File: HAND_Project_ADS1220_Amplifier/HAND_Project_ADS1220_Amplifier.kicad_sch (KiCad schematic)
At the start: 0 parts

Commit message: KiCad
need to assign footprints
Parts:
- added D1, D4: LED, LED_THT:LED_D3.0mm, symbol Device:LED
- added D2, D3: 1N5817, Diode_THT:D_DO-41_SOD81_P10.16mm_Horizontal, symbol Diode:1N5817
- added J1: Screw_Terminal_01x04, symbol Connector:Screw_Terminal_01x04
- added J2, J3: Conn_01x03_Pin, symbol Connector:Conn_01x03_Pin
- added R1, R2: 330, symbol Device:R
- added U1: ADS1220IPWR, ADS1220IPWR:SOP65P640X120-16N, symbol ADS1220IPWR:ADS1220IPWR
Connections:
- new net: D2.1 (K), R1.1, U1.13 (DVDD)
- new net: D1.2 (A), R1.2
- new net: D3.1 (K), R2.1, U1.12 (AVDD)
- new net: J2.1 (Pin_1), U1.1 (SCLK)
- new net: J2.2 (Pin_2), U1.2 (~{CS})
- new net: J2.3 (Pin_3), U1.3 (CLK)
- new net: D4.2 (A), R2.2
- new net: J1.1 (Pin_1), U1.10 (AIN1)
- new net: J1.2 (Pin_2), U1.11 (AIN0/REFP1)
- new net: J3.3 (Pin_3), U1.14 (~{DRDY})
- new net: J3.1 (Pin_1), U1.15 (DOUT/~{DRDY})
- new net: J3.2 (Pin_2), U1.16 (DIN)
- new net 3.3V: D2.2 (A)
- new net 5V: D3.2 (A), J1.4 (Pin_4)
- new net GND: D1.1 (K), D4.1 (K), J1.3 (Pin_3), U1.4 (DGND), U1.5 (AVSS)
- no-connect marks 0 -> 2
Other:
- note added: "4.096MHz PWM 50% Duty Cycle"
- note added: "Pin Connector for Strain Gauge"

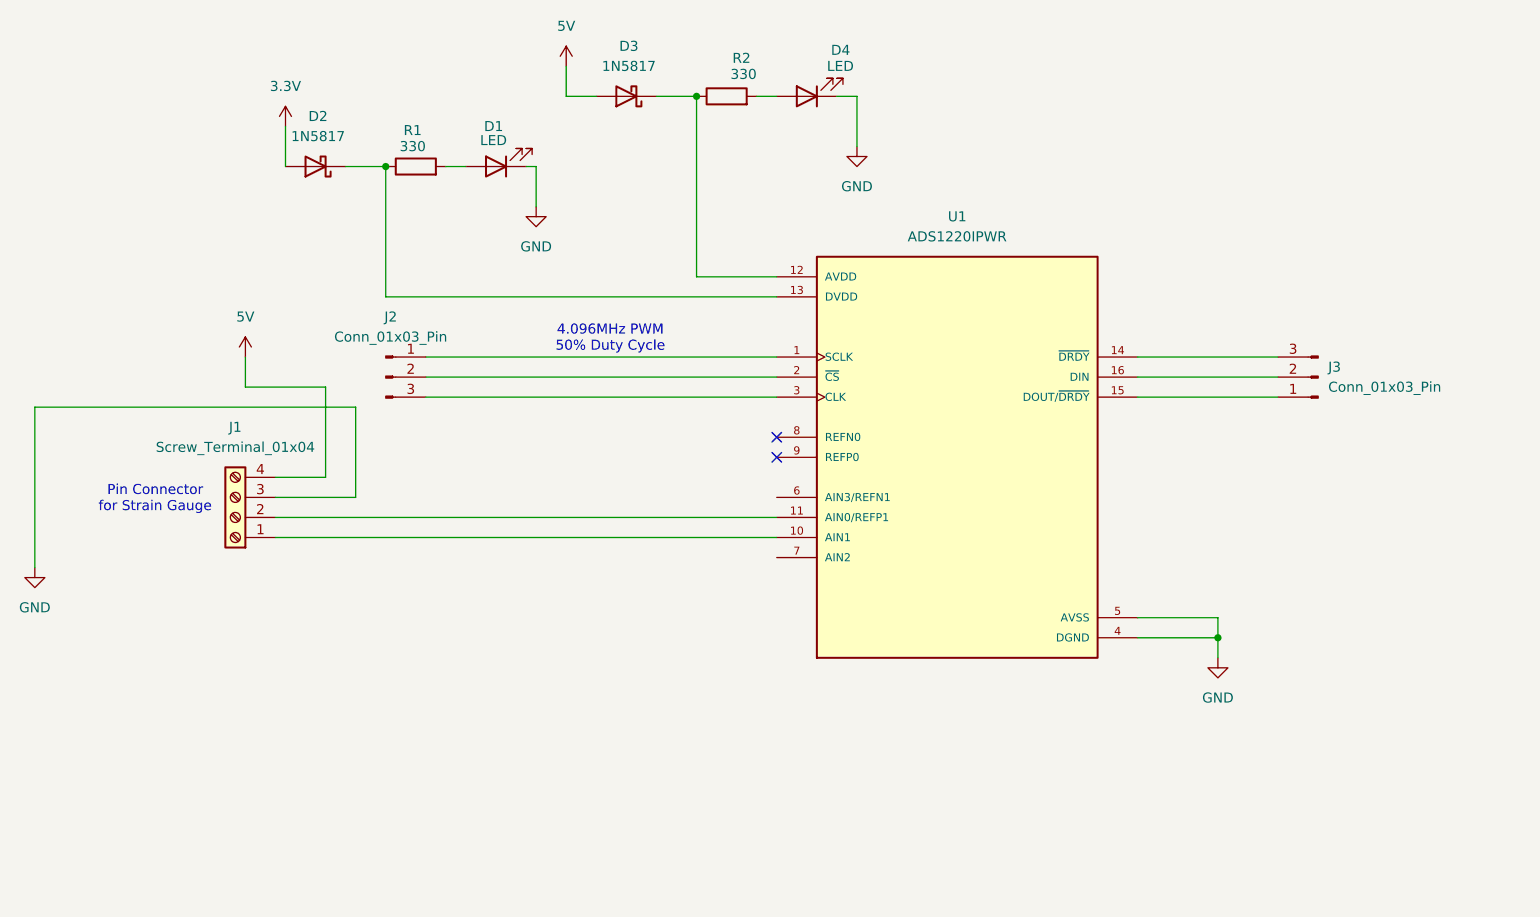
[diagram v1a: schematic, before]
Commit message: Finished schematics + footprints
Need to work on actual PCB design
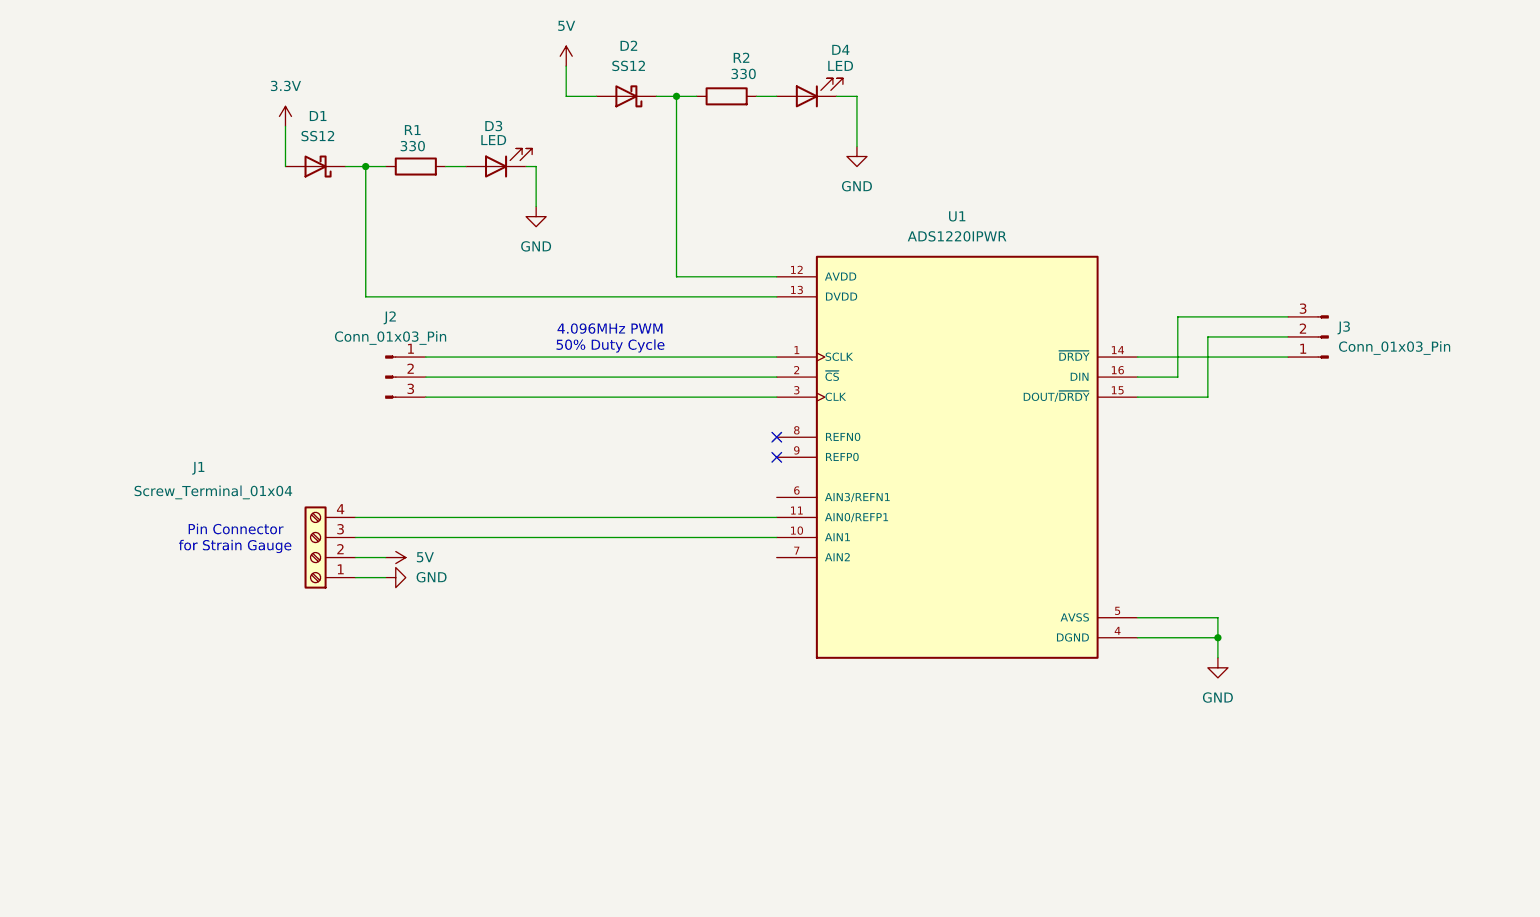
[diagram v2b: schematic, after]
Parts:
- removed D2, D3: 1N5817, Diode_THT:D_DO-41_SOD81_P10.16mm_Horizontal, symbol Diode:1N5817
- added D1, D2: SS12, Diode_SMD:D_SMA, symbol Diode:SS12
- D3: renamed from D1; footprint LED_THT:LED_D3.0mm -> LED_SMD:LED_0603_1608Metric_Pad1.05x0.95mm_HandSolder
- D4: footprint LED_THT:LED_D3.0mm -> LED_SMD:LED_0603_1608Metric_Pad1.05x0.95mm_HandSolder
- J1: footprint (none) -> TerminalBlock_Phoenix:TerminalBlock_Phoenix_MKDS-1,5-4_1x04_P5.00mm_Horizontal
- J2, J3: footprint (none) -> Connector_PinHeader_2.54mm:PinHeader_1x03_P2.54mm_Vertical
- R1, R2: footprint (none) -> Resistor_SMD:R_0603_1608Metric_Pad0.98x0.95mm_HandSolder
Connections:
- net 3.3V: now also D1.2 (A)
- net 5V: now also J1.2 (Pin_2), D2.2 (A); no longer J1.4 (Pin_4)
- net GND: now also J1.1 (Pin_1); no longer J1.3 (Pin_3)
- net at R1.1, U1.13 (DVDD): now also D1.1 (K)
- net at R2.1, U1.12 (AVDD): now also D2.1 (K)
- net at U1.10 (AIN1): now also J1.3 (Pin_3); no longer J1.1 (Pin_1)
- net at U1.11 (AIN0/REFP1): now also J1.4 (Pin_4); no longer J1.2 (Pin_2)
- net at U1.14 (~{DRDY}): now also J3.1 (Pin_1); no longer J3.3 (Pin_3)
- net at U1.15 (DOUT/~{DRDY}): now also J3.2 (Pin_2); no longer J3.1 (Pin_1)
- net at U1.16 (DIN): now also J3.3 (Pin_3); no longer J3.2 (Pin_2)
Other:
- moved on the sheet: J1, J3

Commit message: pin? idk
stuff
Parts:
- J2, J3: footprint Connector_PinHeader_2.54mm:PinHeader_1x03_P2.54mm_Vertical -> Connector_PinSocket_1.00mm:PinSocket_1x03_P1.00mm_Vertical
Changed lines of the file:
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@@
 			)
 		)
-		(property "Footprint" "Connector_PinHeader_2.54mm:PinHeader_1x03_P2.54mm_Vertical"
+		(property "Footprint" "Connector_PinSocket_1.00mm:PinSocket_1x03_P1.00mm_Vertical"
 			(at 76.2 78.74 0)
 			(effects
@@
 			)
 		)
-		(property "Footprint" "Connector_PinHeader_2.54mm:PinHeader_1x03_P2.54mm_Vertical"
+		(property "Footprint" "Connector_PinSocket_1.00mm:PinSocket_1x03_P1.00mm_Vertical"
 			(at 195.58 73.66 0)
 			(effects

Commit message: 4 PM meeting
stuff
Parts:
- added J4: Conn_01x03_Pin, Connector:FanPinHeader_1x03_P2.54mm_Vertical, symbol Connector:Conn_01x03_Pin
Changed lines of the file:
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@@
+	)
+	(symbol
+		(lib_id "Connector:Conn_01x03_Pin")
+		(at 210.82 92.71 0)
+		(unit 1)
+		(exclude_from_sim no)
+		(in_bom yes)
+		(on_board yes)
+		(dnp no)
+		(fields_autoplaced yes)
+		(property "Reference" "J4"
+			(at 211.455 85.09 0)
+			(effects
+				(font
+					(size 1.27 1.27)
+				)
+			)
+		)
+		(property "Value" "Conn_01x03_Pin"
+			(at 211.455 87.63 0)
+			(effects
+				(font
+					(size 1.27 1.27)
+				)
+			)
+		)
+		(property "Footprint" "Connector:FanPinHeader_1x03_P2.54mm_Vertical"
+			(at 210.82 92.71 0)
+			(effects
+				(font
+					(size 1.27 1.27)
+				)
+				(hide yes)
+			)
+		)
+		(property "Datasheet" "~"
+			(at 210.82 92.71 0)
+			(effects
+				(font
+					(size 1.27 1.27)
+				)
+				(hide yes)
+			)
+		)
+		(property "Description" "Generic connector, single row, 01x03, script generated"
+			(at 210.82 92.71 0)
+			(effects
+				(font
+					(size 1.27 1.27)
+				)
+				(hide yes)
+			)
+		)
+		(pin "3"
+		)
+		(pin "1"
+		)
+		(pin "2"
+		)
+		(instances
+			(project ""
+				(path "/f939b9ff-c66a-4ae1-bae0-ab02f1d8a589"
+					(reference "J4")
+					(unit 1)
+				)
+			)
+		)
 	)
 	(symbol

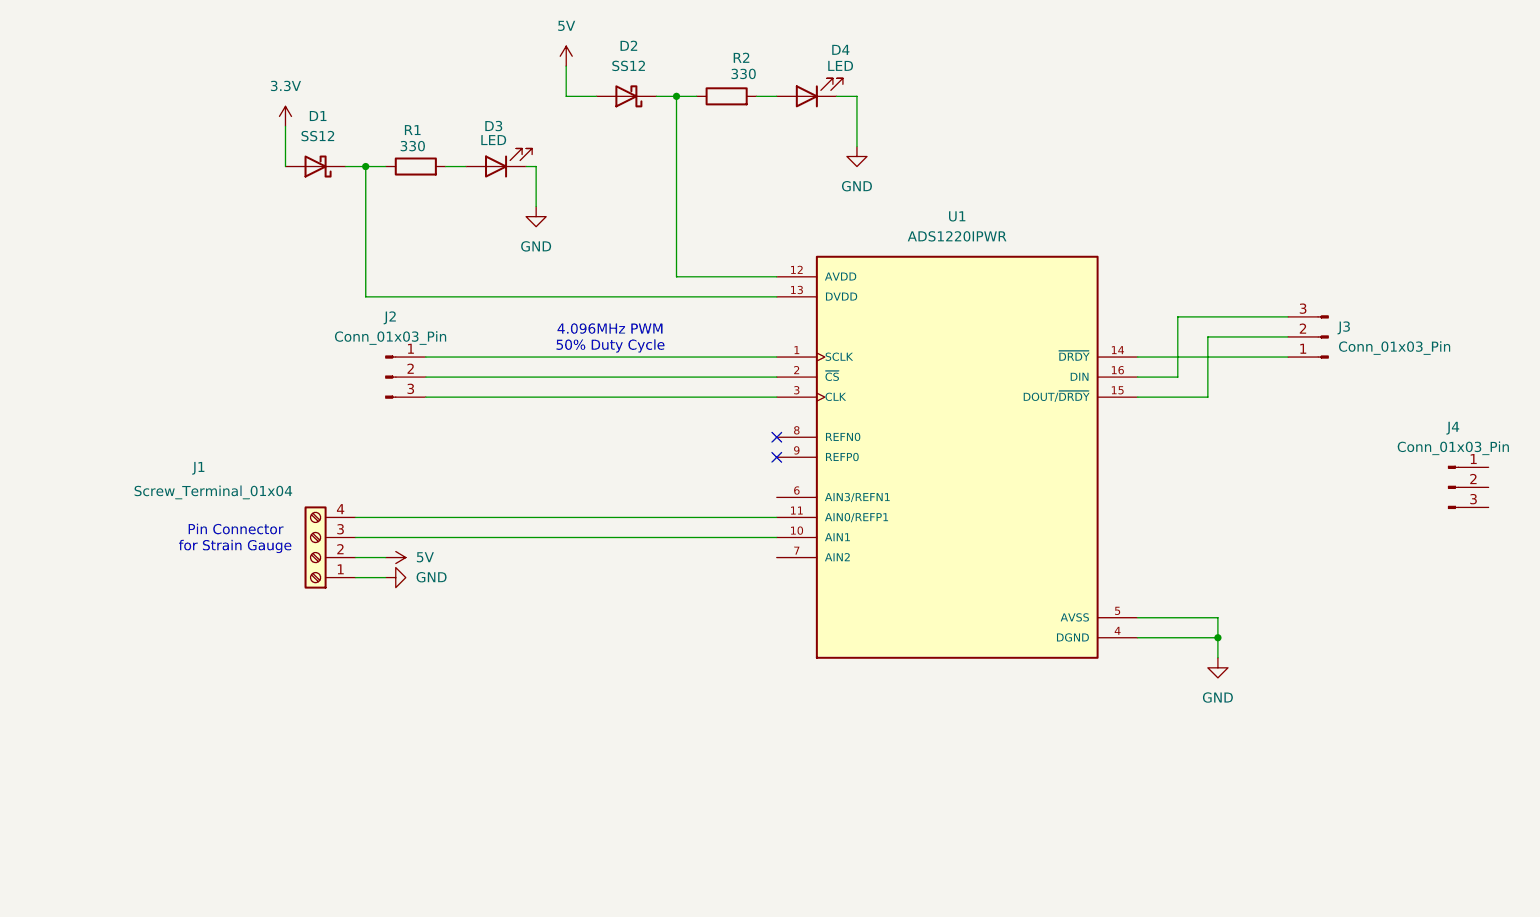
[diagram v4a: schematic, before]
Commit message: Added Pin and Decoupling Capacitors + Fixed PCB version issue
PCB version was a bit messed up because Yuchan and I merged 2 of them together. Have to work on this project at different times if working remotely.
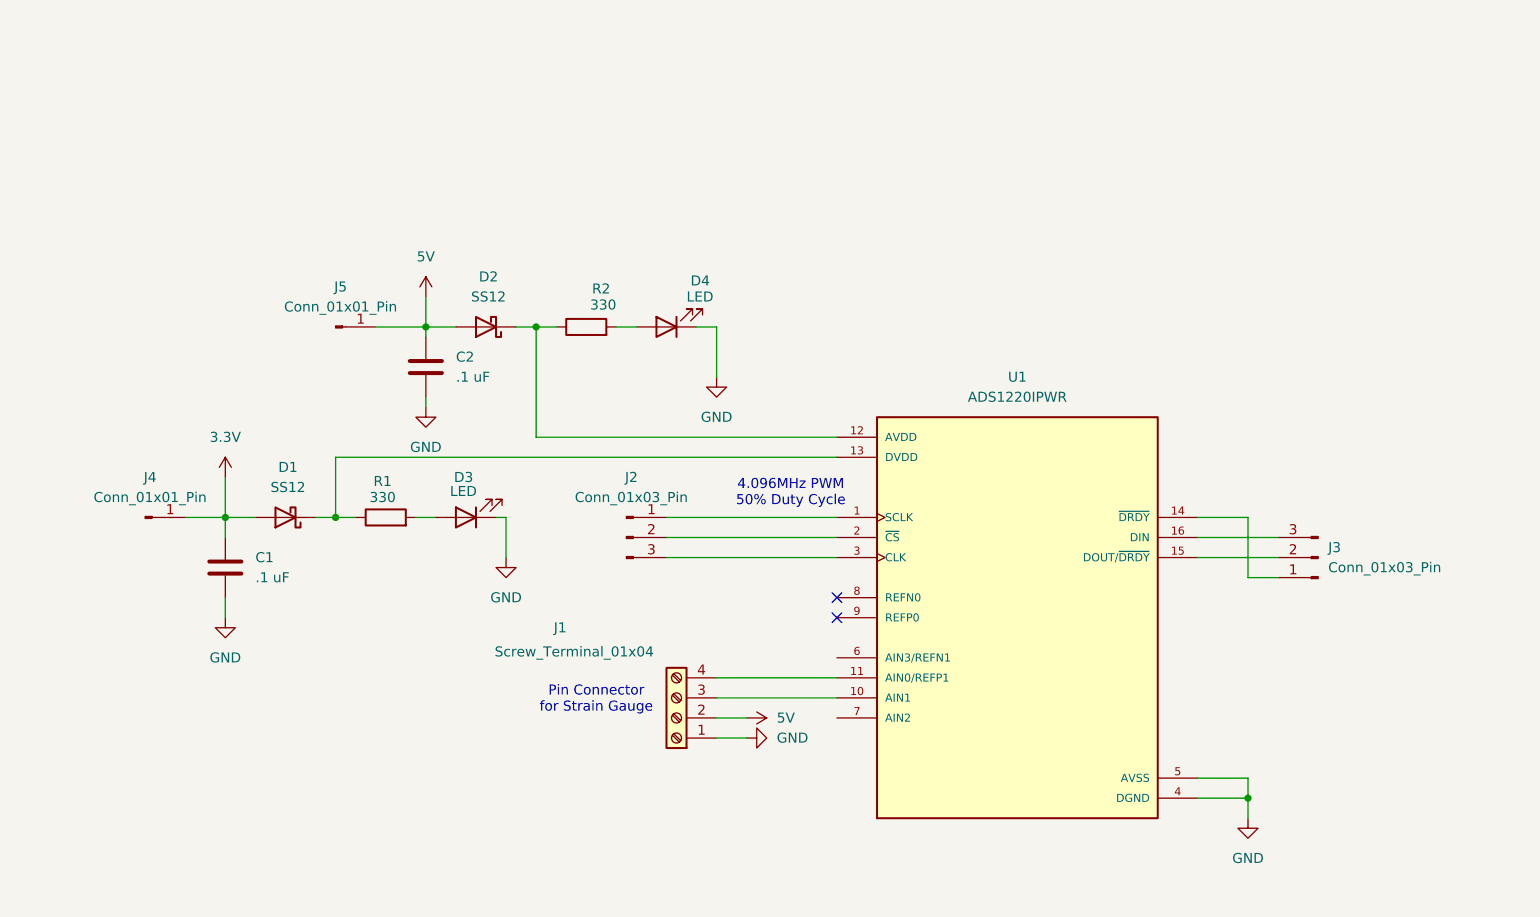
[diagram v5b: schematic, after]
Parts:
- removed J4: Conn_01x03_Pin, Connector:FanPinHeader_1x03_P2.54mm_Vertical, symbol Connector:Conn_01x03_Pin
- added C1, C2: .1 uF, Capacitor_SMD:C_0603_1608Metric_Pad1.08x0.95mm_HandSolder, symbol Device:C
- added J4, J5: Conn_01x01_Pin, Connector_PinSocket_2.54mm:PinSocket_1x01_P2.54mm_Vertical, symbol Connector:Conn_01x01_Pin
- J2, J3: footprint Connector_PinSocket_1.00mm:PinSocket_1x03_P1.00mm_Vertical -> Connector_PinSocket_2.54mm:PinSocket_1x03_P2.54mm_Vertical
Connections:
- net 3.3V: now also C1.1, J4.1 (Pin_1)
- net 5V: now also C2.1, J5.1 (Pin_1)
- net GND: now also C1.2, C2.2
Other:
- company: (none) -> Northwestern HAND ERC
- title: (none) -> ADS1220_Amplifier
- moved on the sheet: D1, D2, D3, D4, J1, J2, J3, R1, R2, U1

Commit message: Attempted to trace PCB... became very confused
Attempting to trace PCB was very difficult. I think I may need to use more vias and perhaps the underside of the board as well because my components are surface mounted.
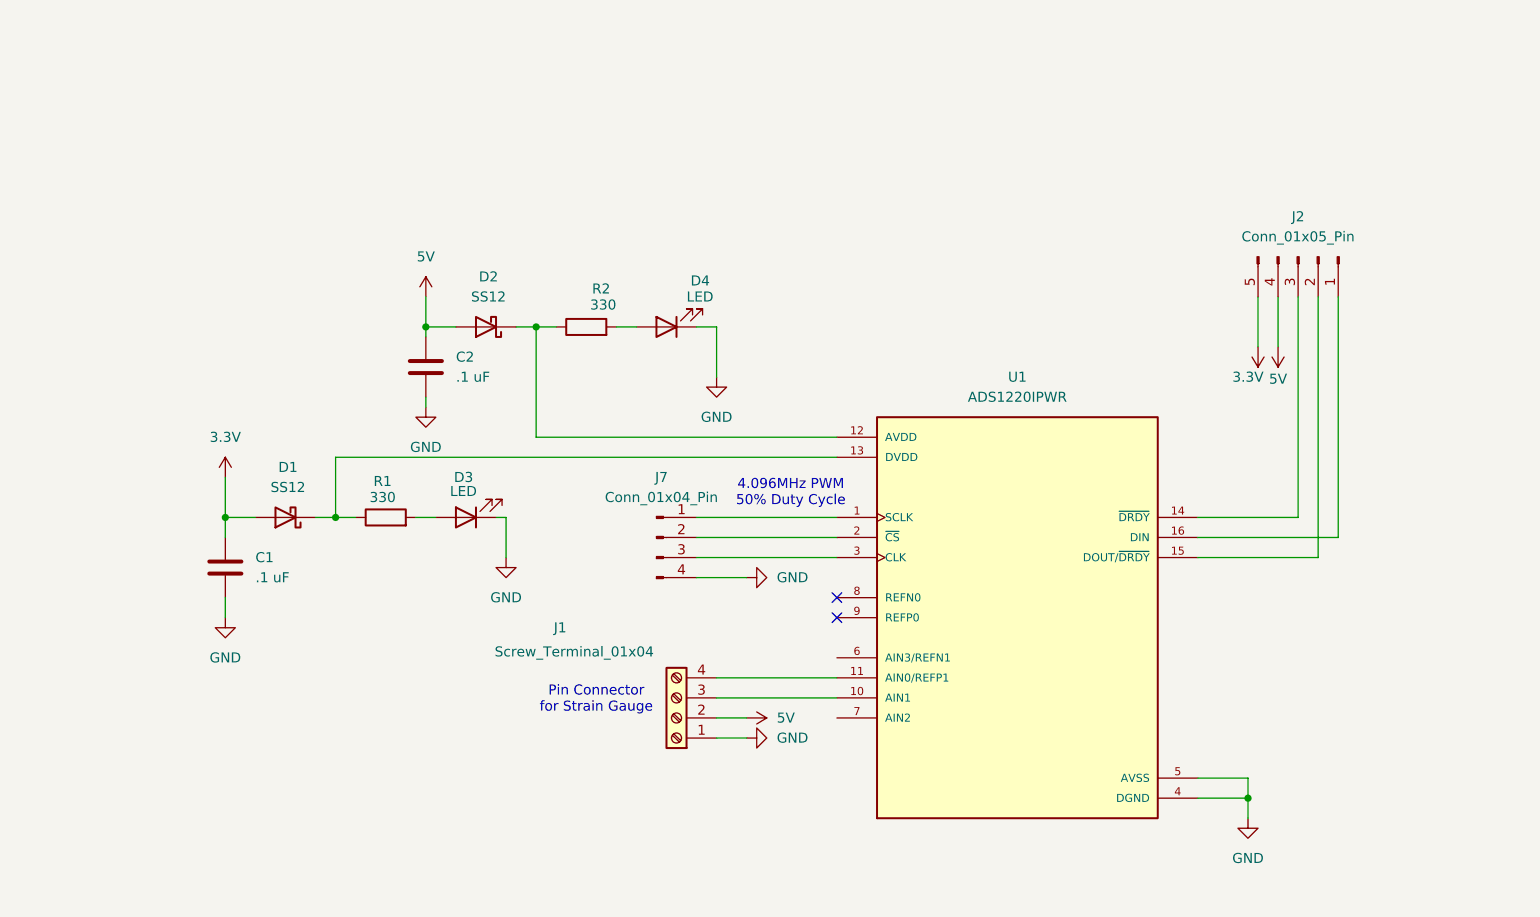
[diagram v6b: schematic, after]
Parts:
- removed J2, J3: Conn_01x03_Pin, Connector_PinSocket_2.54mm:PinSocket_1x03_P2.54mm_Vertical, symbol Connector:Conn_01x03_Pin
- removed J4, J5: Conn_01x01_Pin, Connector_PinSocket_2.54mm:PinSocket_1x01_P2.54mm_Vertical, symbol Connector:Conn_01x01_Pin
- added J2: Conn_01x05_Pin, Connector_PinHeader_2.54mm:PinHeader_1x05_P2.54mm_Vertical, symbol Connector:Conn_01x05_Pin
- added J7: Conn_01x04_Pin, Connector_PinHeader_2.54mm:PinHeader_1x04_P2.54mm_Vertical, symbol Connector:Conn_01x04_Pin
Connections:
- net 3.3V: now also J2.5 (Pin_5)
- net 5V: now also J2.4 (Pin_4)
- net GND: now also J7.4 (Pin_4)
- net at U1.1 (SCLK): now also J7.1 (Pin_1)
- net at U1.2 (~{CS}): now also J7.2 (Pin_2)
- net at U1.3 (CLK): now also J7.3 (Pin_3)
- net at U1.14 (~{DRDY}): now also J2.3 (Pin_3)
- net at U1.15 (DOUT/~{DRDY}): now also J2.2 (Pin_2)
- net at U1.16 (DIN): now also J2.1 (Pin_1)
